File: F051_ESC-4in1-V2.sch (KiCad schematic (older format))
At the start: 39 parts, among them J1 Conn_01x02, J11 Conn_01x03, J14 Conn_01x03, J2 Conn_01x10, J3 Conn_01x05, J4 Conn_01x05, J5 Conn_01x05, J6 Conn_01x03, J7 Conn_01x05, J8 Conn_01x03, J9 Conn_01x10

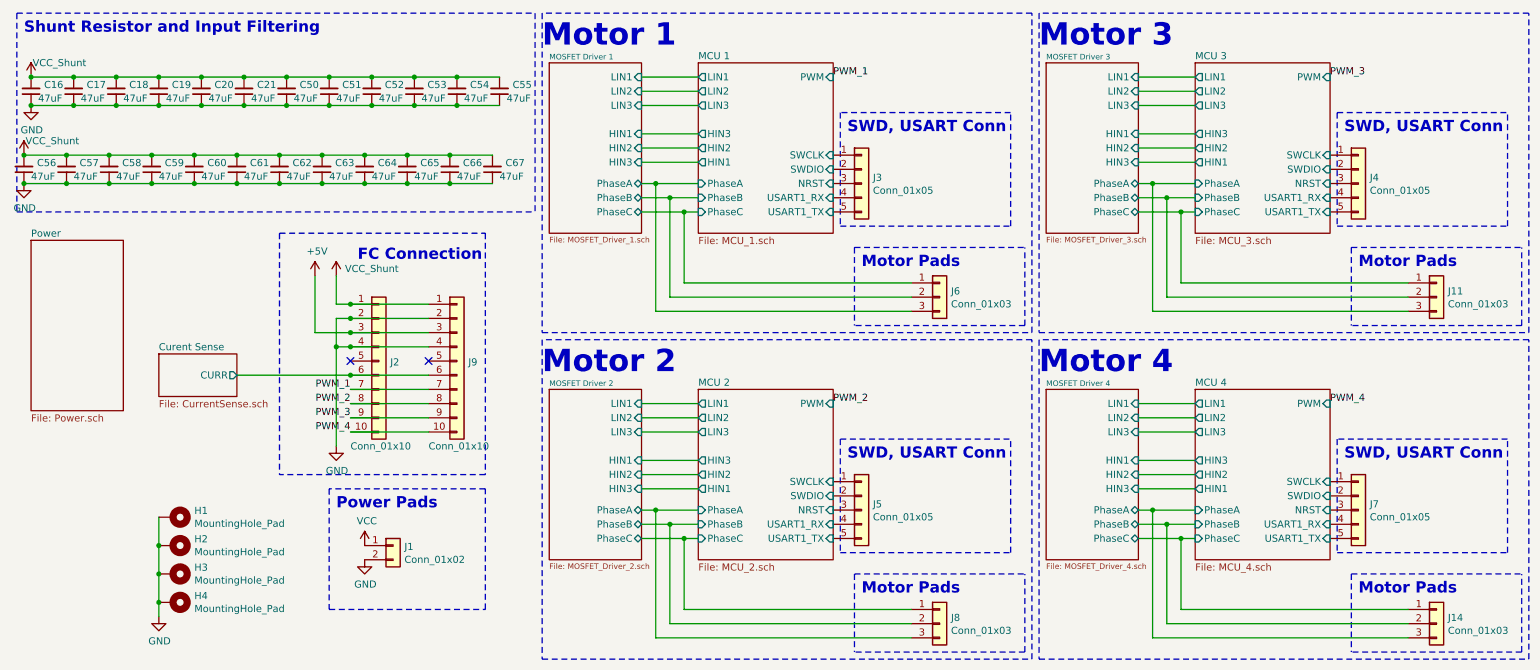
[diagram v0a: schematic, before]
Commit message: Lots of changes made with back being rerouted
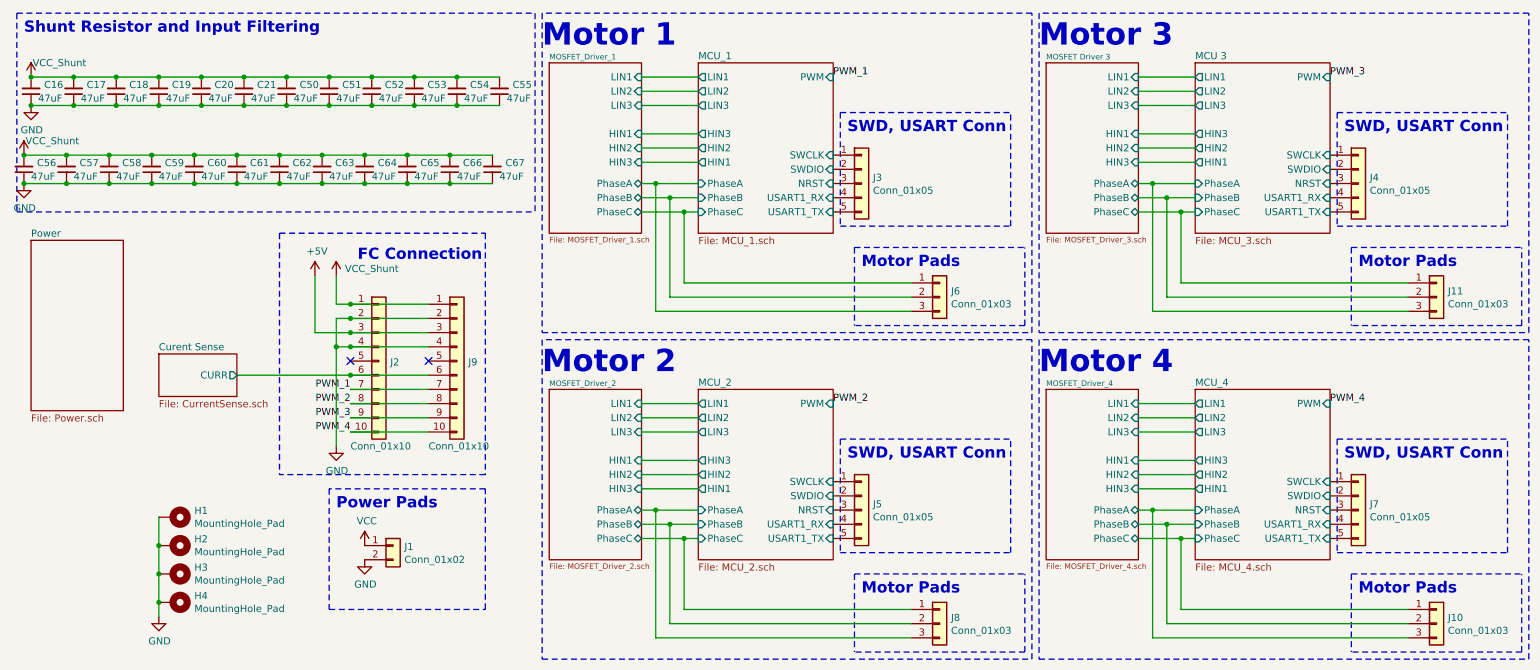
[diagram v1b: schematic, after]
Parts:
- removed J14: Conn_01x03, Connector_Wire:Conn_MotorPhase, symbol Connector_Generic:Conn_01x03
- added J10: Conn_01x03, Connector_Wire:Conn_MotorPhase, symbol Connector_Generic:Conn_01x03
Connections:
- net MCU 1/NRST renamed MCU_1/NRST
- net MCU 1/PhaseA renamed MCU_1/PhaseA
- net MCU 1/PhaseB renamed MCU_1/PhaseB
- net MCU 1/PhaseC renamed MCU_1/PhaseC
- net MCU 1/SWCLK renamed MCU_1/SWCLK
- net MCU 1/SWDIO renamed MCU_1/SWDIO
- net MCU 1/USART1_RX renamed MCU_1/USART1_RX
- net MCU 1/USART1_TX renamed MCU_1/USART1_TX
- net MCU 2/NRST renamed MCU_2/NRST
- net MCU 2/PhaseA renamed MCU_2/PhaseA
- net MCU 2/PhaseB renamed MCU_2/PhaseB
- net MCU 2/PhaseC renamed MCU_2/PhaseC
- net MCU 2/SWCLK renamed MCU_2/SWCLK
- net MCU 2/SWDIO renamed MCU_2/SWDIO
- net MCU 2/USART1_RX renamed MCU_2/USART1_RX
- net MCU 2/USART1_TX renamed MCU_2/USART1_TX
- net MCU 4/NRST renamed MCU_4/NRST
- net MCU 4/SWCLK renamed MCU_4/SWCLK
- net MCU 4/SWDIO renamed MCU_4/SWDIO
- net MCU 4/USART1_RX renamed MCU_4/USART1_RX
- net MCU 4/USART1_TX renamed MCU_4/USART1_TX
- new net MCU_4/PhaseA: J10.3 (Pin_3)
- new net MCU_4/PhaseB: J10.2 (Pin_2)
- new net MCU_4/PhaseC: J10.1 (Pin_1)

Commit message: Lots of routing done to get rid of no-connects.  Down to 35 or so
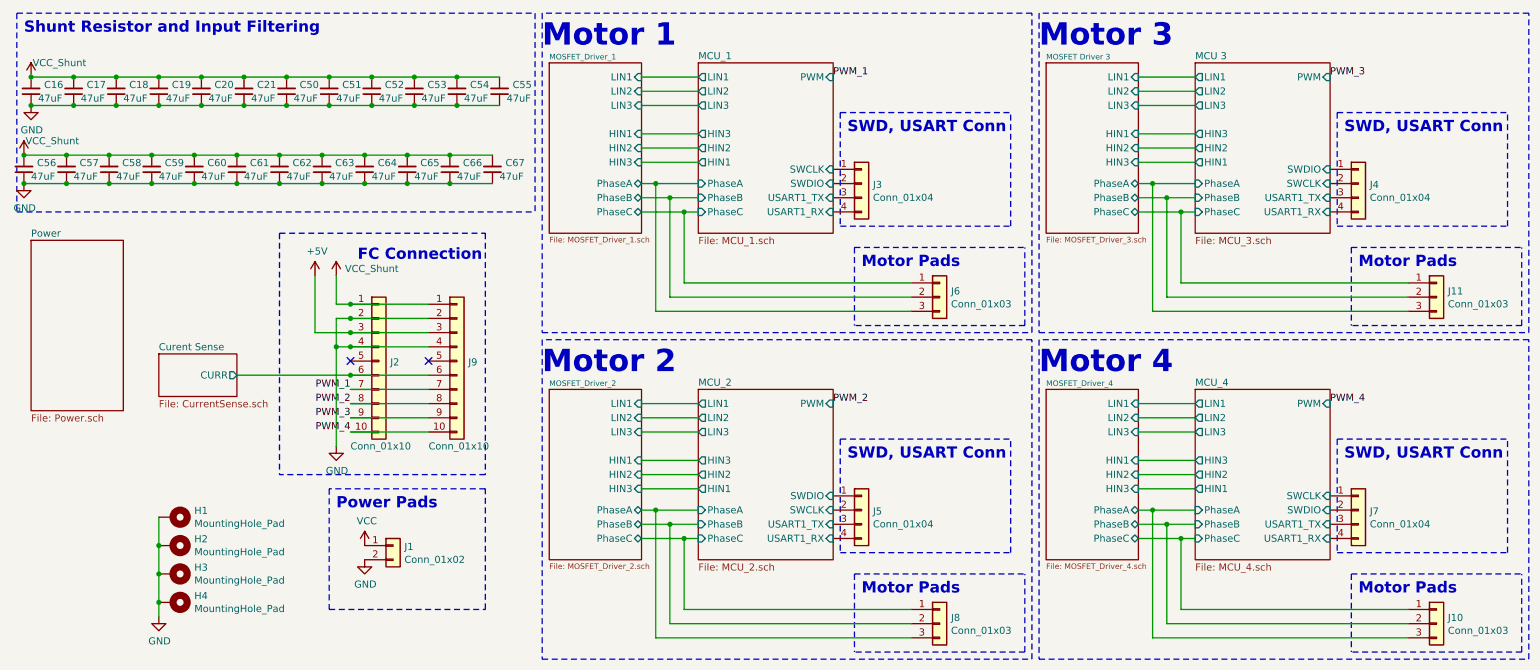
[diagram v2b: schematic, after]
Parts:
- removed J3, J4, J5, J7: Conn_01x05, Connector_Wire:Conn_Debug, symbol Connector_Generic:Conn_01x05
- added J3, J4, J5, J7: Conn_01x04, Connector_Wire:Conn_Debug, symbol Connector_Generic:Conn_01x04
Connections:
- net MCU 3/SWCLK: now also J4.2 (Pin_2)
- net MCU 3/SWDIO: now also J4.1 (Pin_1)
- net MCU 3/USART1_RX: now also J4.4 (Pin_4)
- net MCU 3/USART1_TX: now also J4.3 (Pin_3)
- net MCU_1/SWCLK: now also J3.1 (Pin_1)
- net MCU_1/SWDIO: now also J3.2 (Pin_2)
- net MCU_1/USART1_RX: now also J3.4 (Pin_4)
- net MCU_1/USART1_TX: now also J3.3 (Pin_3)
- net MCU_2/SWCLK: now also J5.2 (Pin_2)
- net MCU_2/SWDIO: now also J5.1 (Pin_1)
- net MCU_2/USART1_RX: now also J5.4 (Pin_4)
- net MCU_2/USART1_TX: now also J5.3 (Pin_3)
- net MCU_4/SWCLK: now also J7.1 (Pin_1)
- net MCU_4/SWDIO: now also J7.2 (Pin_2)
- net MCU_4/USART1_RX: now also J7.4 (Pin_4)
- net MCU_4/USART1_TX: now also J7.3 (Pin_3)

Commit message: Added stuff
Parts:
- added U15: DTOM, Footprints:DTOM_L, symbol JPW_Symbols:DTOM
- J2: footprint Connector_JST:JST_SHL_SM10B-SHLS-TF_1x10-1MP_P1.00mm_Horizontal -> Connector_JST:JST_SH_SM10B-SRSS-TB_1x10-1MP_P1.00mm_Horizontal
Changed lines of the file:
@@
 F 0 "J2" H 3130 2992 50  0000 L CNN
 F 1 "Conn_01x10" H 2850 2400 50  0000 L CNN
-F 2 "Connector_JST:JST_SHL_SM10B-SHLS-TF_1x10-1MP_P1.00mm_Horizontal" H 3050 3000 50  0001 C CNN
+F 2 "Connector_JST:JST_SH_SM10B-SRSS-TB_1x10-1MP_P1.00mm_Horizontal" H 3050 3000 50  0001 C CNN
 F 3 "~" H 3050 3000 50  0001 C CNN
 	1    3050 3000
@@
 F15 "USART1_RX" I R 9750 4250 50
 $EndSheet
+$Comp
+L JPW_Symbols:DTOM U15
+U 1 1 607373EC
+P 950 4150
+F 0 "U15" H 975 4196 50  0000 L CNN
+F 1 "DTOM" H 975 4105 50  0000 L CNN
+F 2 "Footprints:DTOM_L" H 950 4150 50  0001 C CNN
+F 3 "" H 950 4150 50  0001 C CNN
+	1    950  4150
+	1    0    0    -1
+$EndComp
 $EndSCHEMATC
